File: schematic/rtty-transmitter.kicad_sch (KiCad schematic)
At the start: 62 parts, among them J1 USB_B, J2 USBasp header, J3 Conn_Coaxial, Q1 PN2222A, Q2 PN2222A, U1 MCP2221AxP, U2 ATmega328P-P, U3 MCP4901, U4 MCP6022, U5 2x5 Pin Header Connector Fema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

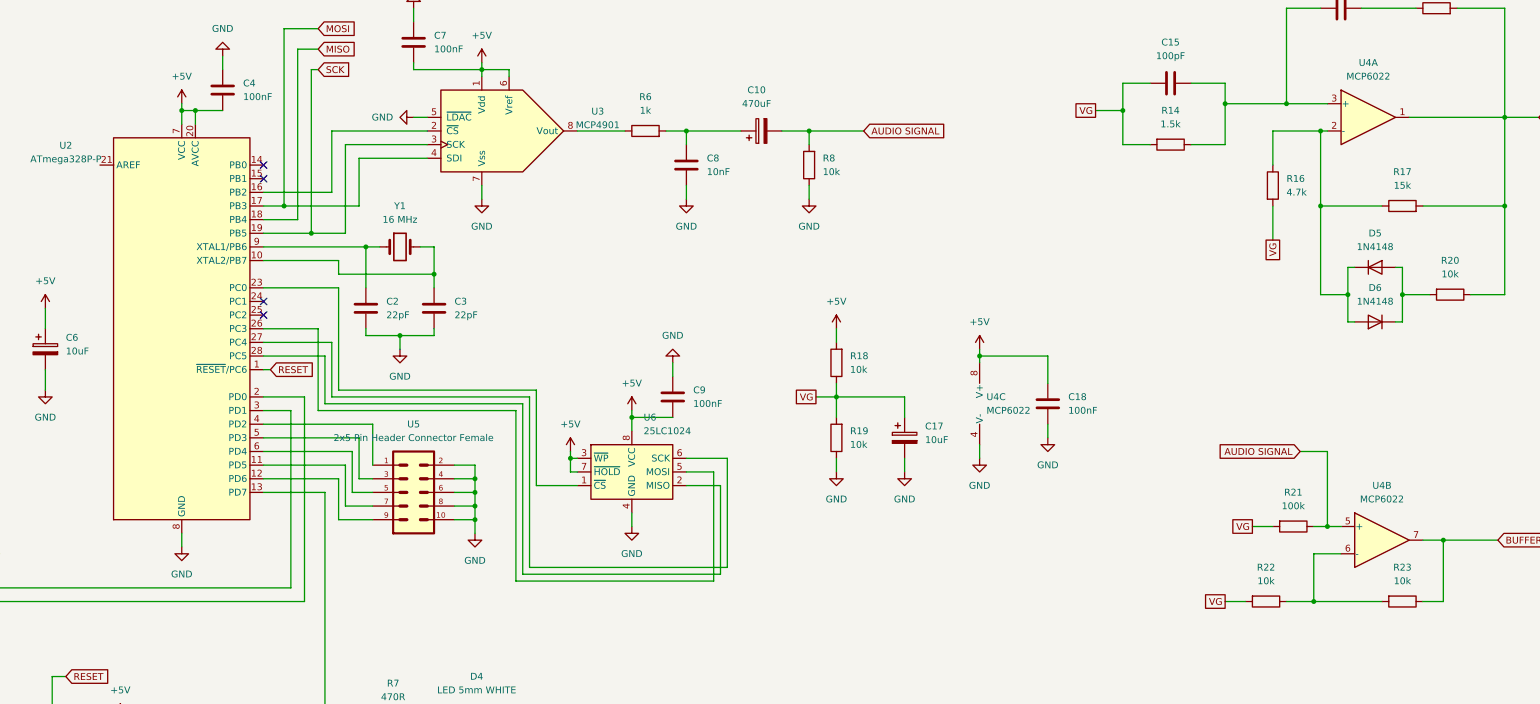
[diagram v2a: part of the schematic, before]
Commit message: Schematic: op-amp audio buffer refined
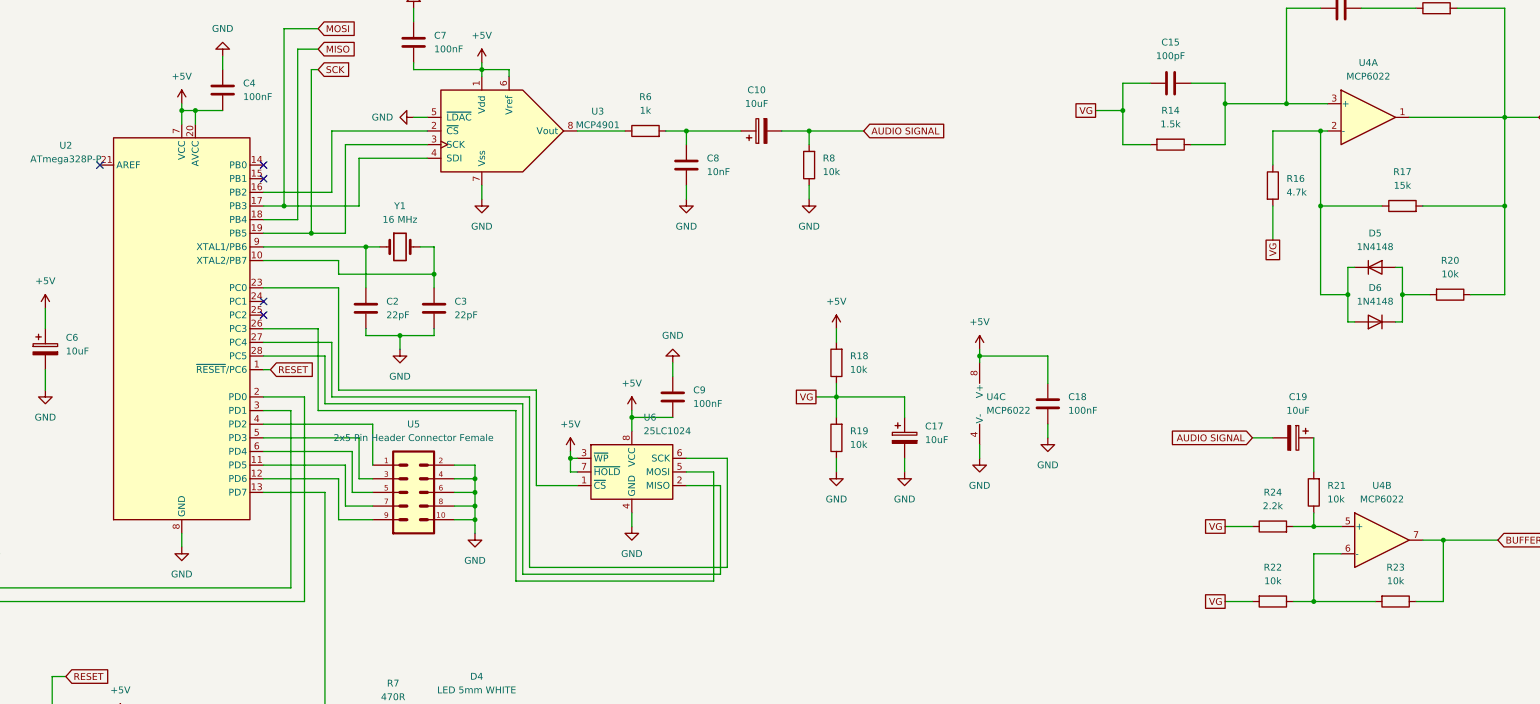
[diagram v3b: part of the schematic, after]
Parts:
- added C19: 10uF, Capacitor_THT:CP_Radial_D6.3mm_P2.50mm, symbol Device:C_Polarized
- added R24: 2.2k, StockLib:R_10k_Axial_DIN0207, symbol StockLib:R_10k
- C10: value 470uF -> 10uF
- R21: value 100k -> 10k
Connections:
- net AUDIO SIGNAL: now also C19.2; no longer R21.1, U4.5 (+)
- net VG: now also R24.1; no longer R21.2
- new net: C19.1, R21.2
- new net: R21.1, R24.2, U4.5 (+)
- no-connect marks 13 -> 14
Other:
- moved on the sheet: R22, R23
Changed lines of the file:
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@@
   (junction (at 29.21 81.28) (diameter 0) (color 0 0 0 0)
   )
+  (junction (at 339.09 121.92) (diameter 0) (color 0 0 0 0)
+  )
   (junction (at 182.88 115.57) (diameter 0) (color 0 0 0 0)
   )
@@
   (junction (at 276.86 90.17) (diameter 0) (color 0 0 0 0)
   )
-  (junction (at 341.63 121.92) (diameter 0) (color 0 0 0 0)
-  )
   (junction (at 162.56 69.85) (diameter 0) (color 0 0 0 0)
   )
@@
   (no_connect (at 73.66 87.63))
   (no_connect (at 143.51 82.55))
+  (no_connect (at 113.03 54.61))
   (no_connect (at 73.66 67.31))
   (no_connect (at 73.66 82.55))
@@
     (stroke (width 0) (type default))
   )
-  (wire (pts (xy 341.63 107.95) (xy 341.63 121.92))
-    (stroke (width 0) (type default))
-  )
   (wire (pts (xy 179.07 110.49) (xy 182.88 110.49))
     (stroke (width 0) (type default))
@@
     (stroke (width 0) (type default))
   )
-  (wire (pts (xy 327.66 121.92) (xy 331.47 121.92))
+  (wire (pts (xy 322.58 121.92) (xy 327.66 121.92))
     (stroke (width 0) (type default))
   )
@@
     (stroke (width 0) (type default))
   )
+  (wire (pts (xy 339.09 119.38) (xy 339.09 121.92))
+    (stroke (width 0) (type default))
+  )
   (wire (pts (xy 311.15 195.58) (xy 311.15 198.12))
     (stroke (width 0) (type default))
@@
     (stroke (width 0) (type default))
   )
-  (wire (pts (xy 334.01 135.89) (xy 339.09 135.89))
+  (wire (pts (xy 335.28 135.89) (xy 339.09 135.89))
     (stroke (width 0) (type default))
   )
@@
     (stroke (width 0) (type default))
   )
+  (wire (pts (xy 339.09 105.41) (xy 339.09 111.76))
+    (stroke (width 0) (type default))
+  )
   (wire (pts (xy 44.45 170.18) (xy 44.45 172.72))
     (stroke (width 0) (type default))
@@
     (stroke (width 0) (type default))
   )
-  (wire (pts (xy 322.58 135.89) (xy 326.39 135.89))
+  (wire (pts (xy 322.58 135.89) (xy 327.66 135.89))
     (stroke (width 0) (type default))
   )
@@
     (stroke (width 0) (type default))
   )
-  (wire (pts (xy 359.41 135.89) (xy 363.22 135.89))
+  (wire (pts (xy 358.14 135.89) (xy 363.22 135.89))
     (stroke (width 0) (type default))
   )
@@
     (stroke (width 0) (type default))
   )
-  (wire (pts (xy 339.09 121.92) (xy 341.63 121.92))
+  (wire (pts (xy 339.09 121.92) (xy 344.17 121.92))
     (stroke (width 0) (type default))
   )
@@
     (stroke (width 0) (type default))
   )
+  (wire (pts (xy 327.66 105.41) (xy 331.47 105.41))
+    (stroke (width 0) (type default))
+  )
   (wire (pts (xy 143.51 107.95) (xy 160.02 107.95))
     (stroke (width 0) (type default))
@@
     (stroke (width 0) (type default))
   )
-  (wire (pts (xy 339.09 135.89) (xy 351.79 135.89))
+  (wire (pts (xy 339.09 135.89) (xy 350.52 135.89))
     (stroke (width 0) (type default))
   )
@@
     (stroke (width 0) (type default))
   )
+  (wire (pts (xy 335.28 121.92) (xy 339.09 121.92))
+    (stroke (width 0) (type default))
+  )
   (wire (pts (xy 355.6 181.61) (xy 355.6 179.07))
     (stroke (width 0) (type default))
@@
     (stroke (width 0) (type default))
   )
-  (wire (pts (xy 336.55 107.95) (xy 341.63 107.95))
-    (stroke (width 0) (type default))
-  )
   (wire (pts (xy 184.15 36.83) (xy 184.15 38.1))
     (stroke (width 0) (type default))
   )
-  (wire (pts (xy 341.63 121.92) (xy 344.17 121.92))
-    (stroke (width 0) (type default))
-  )
   (wire (pts (xy 340.36 48.26) (xy 340.36 62.23))
     (stroke (width 0) (type default))
@@
     )
   )
-  (global_label "VG" (shape passive) (at 327.66 121.92 180) (fields_autoplaced)
+  (global_label "VG" (shape passive) (at 322.58 121.92 180) (fields_autoplaced)
     (effects (font (size 1.27 1.27)) (justify right))
-    (property "Intersheetrefs" "${INTERSHEET_REFS}" (at 323.4275 121.92 0)
+    (property "Intersheetrefs" "${INTERSHEET_REFS}" (at 318.3475 121.92 0)
       (effects (font (size 1.27 1.27)) (justify right) hide)
     )
   )
-  (global_label "AUDIO SIGNAL" (shape input) (at 336.55 107.95 180) (fields_autoplaced)
+  (global_label "AUDIO SIGNAL" (shape input) (at 327.66 105.41 180) (fields_autoplaced)
     (effects (font (size 1.27 1.27)) (justify right))
-    (property "Intersheetrefs" "${INTERSHEET_REFS}" (at 320.4413 107.95 0)
+    (property "Intersheetrefs" "${INTERSHEET_REFS}" (at 311.5513 105.41 0)
       (effects (font (size 1.27 1.27)) (justify right) hide)
     )
@@
     )
   )
-  (symbol (lib_id "StockLib:R_10k") (at 355.6 135.89 270) (unit 1)
+  (symbol (lib_id "Device:C_Polarized") (at 335.28 105.41 270) (unit 1)
     (in_bom yes) (on_board yes) (dnp no) (fields_autoplaced)
-    (property "Reference" "R23" (at 355.6 129.54 90)
+    (property "Reference" "C19" (at 336.169 97.79 90)
       (effects (font (size 1.27 1.27)))
     )
-    (property "Value" "10k" (at 355.6 132.08 90)
+    (property "Value" "10uF" (at 336.169 100.33 90)
       (effects (font (size 1.27 1.27)))
     )
-    (property "Footprint" "StockLib:R_10k_Axial_DIN0207" (at 355.6 134.112 90)
+    (property "Footprint" "Capacitor_THT:CP_Radial_D6.3mm_P2.50mm" (at 331.47 106.3752 0)
       (effects (font (size 1.27 1.27)) hide)
     )
-    (property "Datasheet" "~" (at 355.6 135.89 0)
+    (property "Datasheet" "~" (at 335.28 105.41 0)
+      (effects (font (size 1.27 1.27)) hide)
+    )
+    (pin "1")
+    (pin "2")
+    (instances
+      (project "rtty-transmitter"
+        (path "/4ea8d87c-4bb0-4c80-84f6-8dbfd2cdcfd6"
+          (reference "C19") (unit 1)
+        )
+      )
+    )
+  )
+  (symbol (lib_id "StockLib:R_10k") (at 354.33 135.89 270) (unit 1)
+    (in_bom yes) (on_board yes) (dnp no) (fields_autoplaced)
+    (property "Reference" "R23" (at 354.33 129.54 90)
+      (effects (font (size 1.27 1.27)))
+    )
+    (property "Value" "10k" (at 354.33 132.08 90)
+      (effects (font (size 1.27 1.27)))
+    )
+    (property "Footprint" "StockLib:R_10k_Axial_DIN0207" (at 354.33 134.112 90)
+      (effects (font (size 1.27 1.27)) hide)
+    )
+    (property "Datasheet" "~" (at 354.33 135.89 0)
       (effects (font (size 1.27 1.27)) hide)
     )
@@
     )
   )
+  (symbol (lib_id "StockLib:R_10k") (at 339.09 115.57 180) (unit 1)
+    (in_bom yes) (on_board yes) (dnp no) (fields_autoplaced)
+    (property "Reference" "R21" (at 341.63 114.3 0)
+      (effects (font (size 1.27 1.27)) (justify right))
+    )
+    (property "Value" "10k" (at 341.63 116.84 0)
+      (effects (font (size 1.27 1.27)) (justify right))
+    )
+    (property "Footprint" "StockLib:R_10k_Axial_DIN0207" (at 340.868 115.57 90)
+      (effects (font (size 1.27 1.27)) hide)
+    )
+    (property "Datasheet" "~" (at 339.09 115.57 0)
+      (effects (font (size 1.27 1.27)) hide)
+    )
+    (pin "1")
+    (pin "2")
+    (instances
+      (project "rtty-transmitter"
+        (path "/4ea8d87c-4bb0-4c80-84f6-8dbfd2cdcfd6"
+          (reference "R21") (unit 1)
+        )
+      )
+    )
+  )
   (symbol (lib_id "StockLib:R_10k") (at 327.66 236.22 180) (unit 1)
     (in_bom yes) (on_board yes) (dnp no) (fields_autoplaced)
@@
     )
   )
-  (symbol (lib_id "StockLib:R_10k") (at 335.28 121.92 270) (unit 1)
-    (in_bom yes) (on_board yes) (dnp no) (fields_autoplaced)
-    (property "Reference" "R21" (at 335.28 115.57 90)
-      (effects (font (size 1.27 1.27)))
-    )
-    (property "Value" "100k" (at 335.28 118.11 90)
-      (effects (font (size 1.27 1.27)))
-    )
-    (property "Footprint" "StockLib:R_10k_Axial_DIN0207" (at 335.28 120.142 90)
-      (effects (font (size 1.27 1.27)) hide)
-    )
-    (property "Datasheet" "~" (at 335.28 121.92 0)
-      (effects (font (size 1.27 1.27)) hide)
-    )
-    (pin "1")
-    (pin "2")
-    (instances
-      (project "rtty-transmitter"
-        (path "/4ea8d87c-4bb0-4c80-84f6-8dbfd2cdcfd6"
-          (reference "R21") (unit 1)
-        )
-      )
-    )
-  )
   (symbol (lib_id "power:GND") (at 212.09 121.92 0) (unit 1)
     (in_bom yes) (on_board yes) (dnp no) (fields_autoplaced)
@@
     )
   )
+  (symbol (lib_id "StockLib:R_10k") (at 331.47 121.92 90) (unit 1)
+    (in_bom yes) (on_board yes) (dnp no) (fields_autoplaced)
+    (property "Reference" "R24" (at 331.47 115.57 90)
+      (effects (font (size 1.27 1.27)))
+    )
+    (property "Value" "2.2k" (at 331.47 118.11 90)
+      (effects (font (size 1.27 1.27)))
+    )
+    (property "Footprint" "StockLib:R_10k_Axial_DIN0207" (at 331.47 123.698 90)
+      (effects (font (size 1.27 1.27)) hide)
+    )
+    (property "Datasheet" "~" (at 331.47 121.92 0)
+      (effects (font (size 1.27 1.27)) hide)
+    )
+    (pin "1")
+    (pin "2")
+    (instances
+      (project "rtty-transmitter"
+        (path "/4ea8d87c-4bb0-4c80-84f6-8dbfd2cdcfd6"
+          (reference "R24") (unit 1)
+        )
+      )
+    )
+  )
   (symbol (lib_id "StockLib:C_100nF") (at 171.45 31.75 0) (unit 1)
     (in_bom yes) (on_board yes) (dnp no) (fields_autoplaced)
@@
       (effects (font (size 1.27 1.27)))
     )
-    (property "Value" "470uF" (at 235.331 43.18 90)
+    (property "Value" "10uF" (at 235.331 43.18 90)
       (effects (font (size 1.27 1.27)))
     )
@@
     )
   )
-  (symbol (lib_id "StockLib:R_10k") (at 330.2 135.89 270) (unit 1)
+  (symbol (lib_id "StockLib:R_10k") (at 331.47 135.89 270) (unit 1)
     (in_bom yes) (on_board yes) (dnp no) (fields_autoplaced)
-    (property "Reference" "R22" (at 330.2 129.54 90)
+    (property "Reference" "R22" (at 331.47 129.54 90)
       (effects (font (size 1.27 1.27)))
     )
-    (property "Value" "10k" (at 330.2 132.08 90)
+    (property "Value" "10k" (at 331.47 132.08 90)
       (effects (font (size 1.27 1.27)))
     )
-    (property "Footprint" "StockLib:R_10k_Axial_DIN0207" (at 330.2 134.112 90)
+    (property "Footprint" "StockLib:R_10k_Axial_DIN0207" (at 331.47 134.112 90)
       (effects (font (size 1.27 1.27)) hide)
     )
-    (property "Datasheet" "~" (at 330.2 135.89 0)
+    (property "Datasheet" "~" (at 331.47 135.89 0)
       (effects (font (size 1.27 1.27)) hide)
     )

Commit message: Schematic: Jumpers added for RX/TX lines, audio output socket added
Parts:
- added J4, J5: Conn_01x02_Pin, Connector_PinHeader_2.54mm:PinHeader_1x02_P2.54mm_Vertical, symbol Connector:Conn_01x02_Pin
- added J6: Conn_01x02_Pin, Connector_PinSocket_2.54mm:PinSocket_1x02_P2.54mm_Vertical, symbol Connector:Conn_01x02_Pin
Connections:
- net +5V: now also C4.1, C9.1; no longer C4.2, C9.2
- net AUDIO SIGNAL: now also J6.1 (Pin_1)
- net GND: now also C4.2, C9.2, J6.2 (Pin_2); no longer C4.1, C9.1
- net at R3.1, U2.3 (PD1): now also J5.1 (Pin_1); no longer U1.5 (URx)
- net at R4.1, U2.2 (PD0): now also J4.2 (Pin_2); no longer U1.6 (UTx)
- new net: J5.2 (Pin_2), U1.5 (URx)
- new net: J4.1 (Pin_1), U1.6 (UTx)
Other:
- moved on the sheet: C1, C10, C11, C12, C13, C14, C15, C16, C17, C18, C19, C2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
